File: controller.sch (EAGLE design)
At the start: 39 parts, among them IC1 7805DT, Q1 MOSFET-PCHANNEL, Q2 MOSFET-NCHANNELBSS123LT1G, Q3 MOSFET-NCHANNELFDD8780, U1 ATMEGA328P, Y1 16MHz

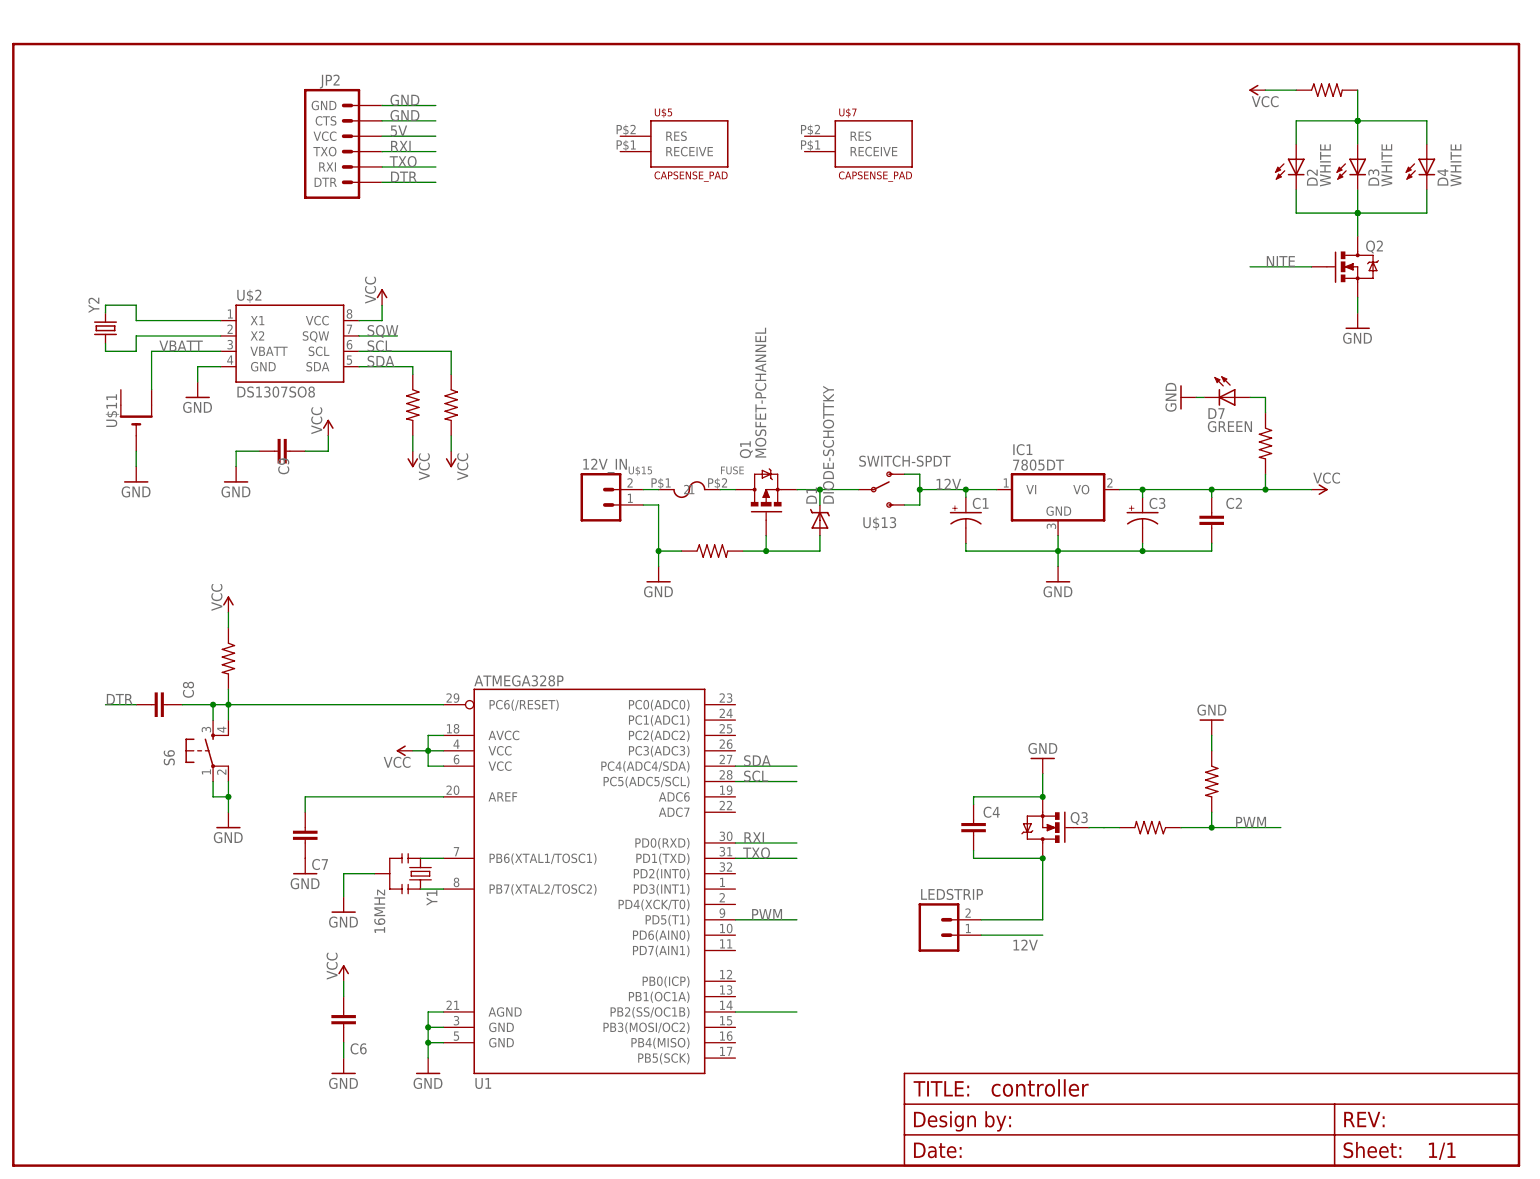
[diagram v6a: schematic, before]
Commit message: changed to one board design.
 added LCD. added capacitive sense IC. changed to SMD programming
header.
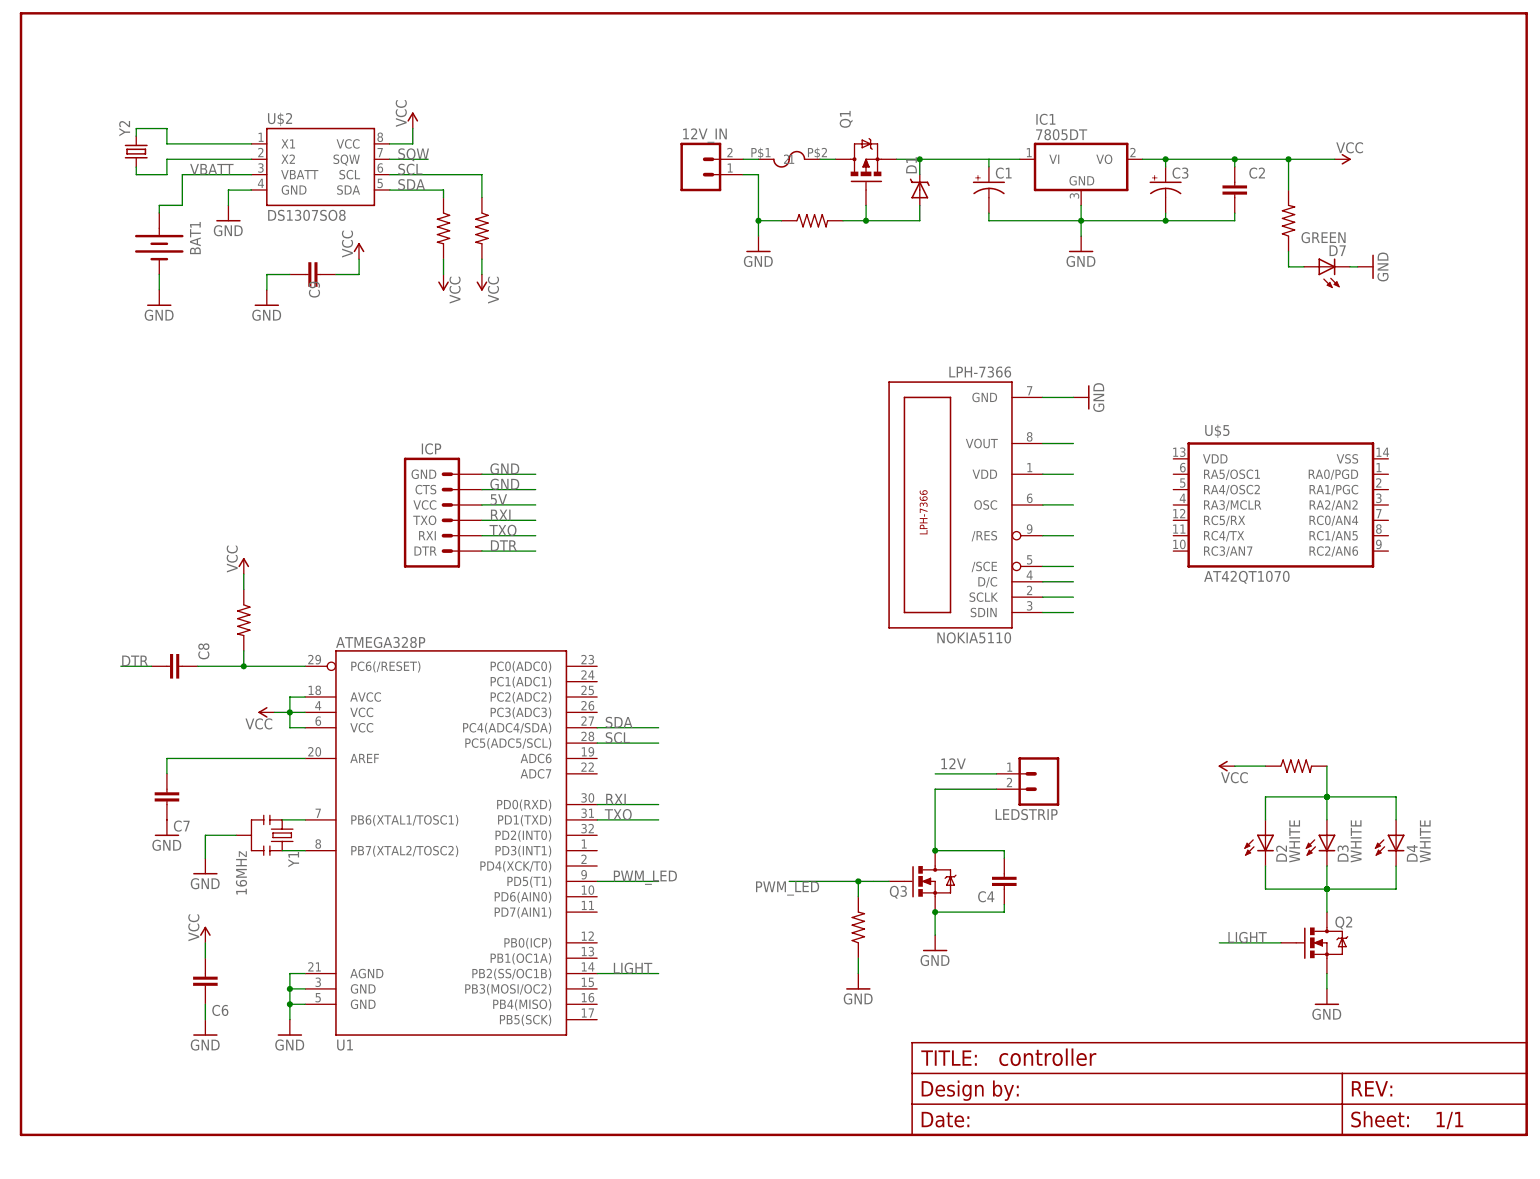
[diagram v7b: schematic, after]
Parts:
- removed FRAME2: FRAME-LETTER, SparkFun-Aesthetics:FRAME-LETTER
- removed JP2: (no value), SparkFun-Connectors:ARDUINO_SERIAL_PROGRAMLOCK
- removed S6: (no value), SparkFun-Electromechanical:TAC_SWITCHSMD
- removed U$11: (no value), adafruit:CR1220THM
- removed U$13: SWITCH-SPDT, jt_parts:SWITCH-SPDT
- removed U$6: (no value), jt_parts:RESISTOR
- removed U$7: CAPSENSE_PAD, SparkFun-Electromechanical:CAPSENSE_PAD
- added BAT1: (no value), SparkFun-Electromechanical:BATTERY12MM
- added ICP: (no value), SparkFun-Connectors:ARDUINO_SERIAL_PROGRAMSMD
- added NOKIA5110: LPH-7366, lph-7366:LPH-7366
- added U$1: FRAME_LETTER, jt_parts:FRAME_LETTER
- Q1: value MOSFET-PCHANNEL -> MOSFET_PCHANNEL; device SparkFun-DiscreteSemi:MOSFET-PCHANNEL -> jt_parts:MOSFET_PCHANNEL
- U$5: value CAPSENSE_PAD -> AT42QT1070; device SparkFun-Electromechanical:CAPSENSE_PAD -> jt_parts:AT42QT1070
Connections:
- net NITE renamed LIGHT
- removed net NONE: U$6.2
- removed net PWM: U$16.2, U$6.1, U1.PD5(T1)
- new net N$17: NOKIA5110.D/C
- new net N$18: NOKIA5110./SCE
- new net N$19: NOKIA5110./RES
- new net N$2: NOKIA5110.SDIN
- new net N$20: NOKIA5110.OSC
- new net N$22: NOKIA5110.VOUT
- new net N$5: NOKIA5110.SCLK
- new net PWM_LED: U$16.2, U1.PD5(T1)
- net 12V: no longer C1.+, IC1.VI, U$13.1, U$13.3
- net 5V: now also ICP.VCC, NOKIA5110.VDD; no longer JP2.VCC
- net DTR: now also ICP.DTR; no longer JP2.DTR
- net GND: now also BAT1.-, ICP.CTS, ICP.GND, NOKIA5110.GND; no longer JP2.CTS, JP2.GND, S6.1, S6.2, U$11.-
- net N$14: now also C1.+, IC1.VI; no longer U$13.2
- net N$15: no longer S6.3, S6.4
- net RXI: now also ICP.TXO; no longer JP2.TXO
- net TXO: now also ICP.RXI; no longer JP2.RXI
- net VBATT: now also BAT1.+; no longer U$11.+1
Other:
- moved on the sheet: 12V_IN, C1, C2, C3, C4, C6, C7, C8, C9, D1, D2, D3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

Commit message: Layed out new power section. Some new digital routing. Added rt angle SMT LEDs.
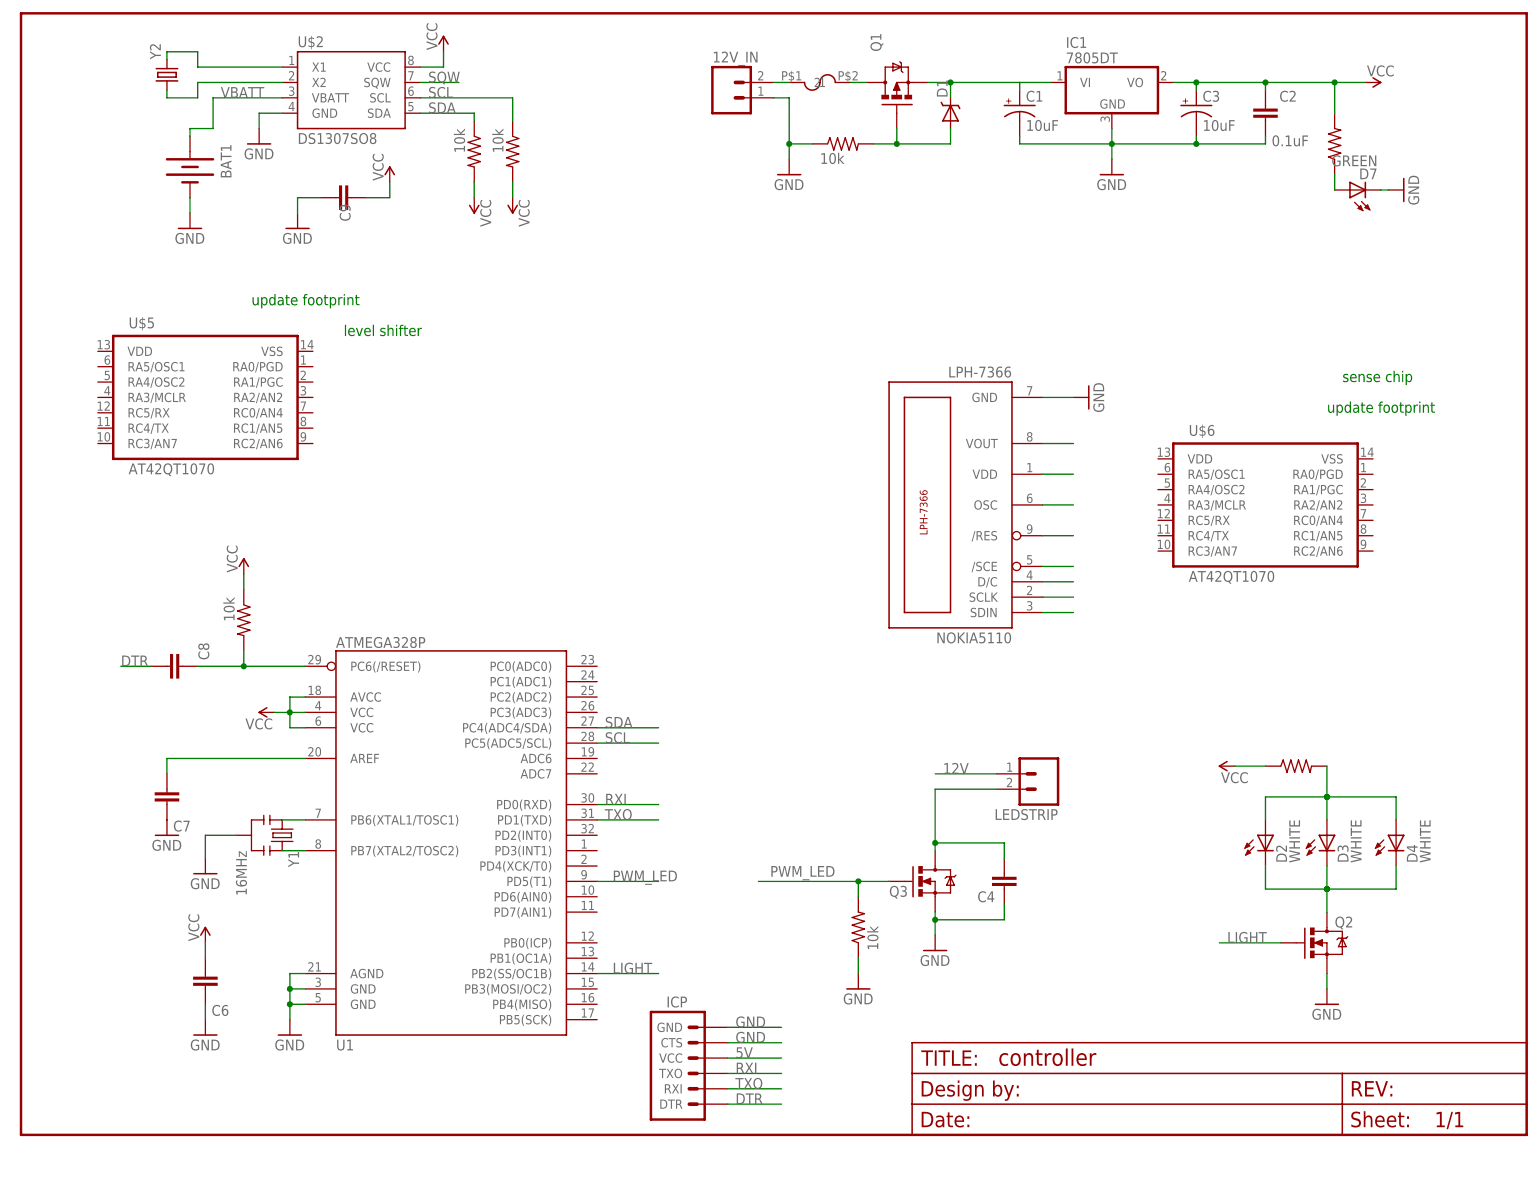
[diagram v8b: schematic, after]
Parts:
- added U$6: AT42QT1070, jt_parts:AT42QT1070
- C1, C3: value (none) -> 10uF
- C2: value (none) -> 0.1uF
- D2, D3, D4: device SparkFun-LED:LED3MM -> adafruit:LEDMICRO-SIDELED
- U$10, U$16, U$17, U$8, U$9: value (none) -> 10k
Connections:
- net 12V-RETURN renamed N$14
- removed net N$14 (its old number): C1.+, D1.C, IC1.VI, Q1.S
- removed net N$3: Q3.G
- net 12V: now also C1.+, D1.C, IC1.VI, Q1.S
- net PWM_LED: now also Q3.G
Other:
- note added: "level shifter"
- note added: "sense chip"
- note added: "update footprint"
- moved on the sheet: 12V_IN, BAT1, C1, C2, C3, C9, D1, D7, IC1, ICP, Q1, U$2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
